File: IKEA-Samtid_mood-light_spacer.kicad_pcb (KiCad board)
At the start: 2 copper layers, 65 x 65 mm, 2 parts, among them P3.1 B-to-B-1A, P4.1 B-to-B-2A

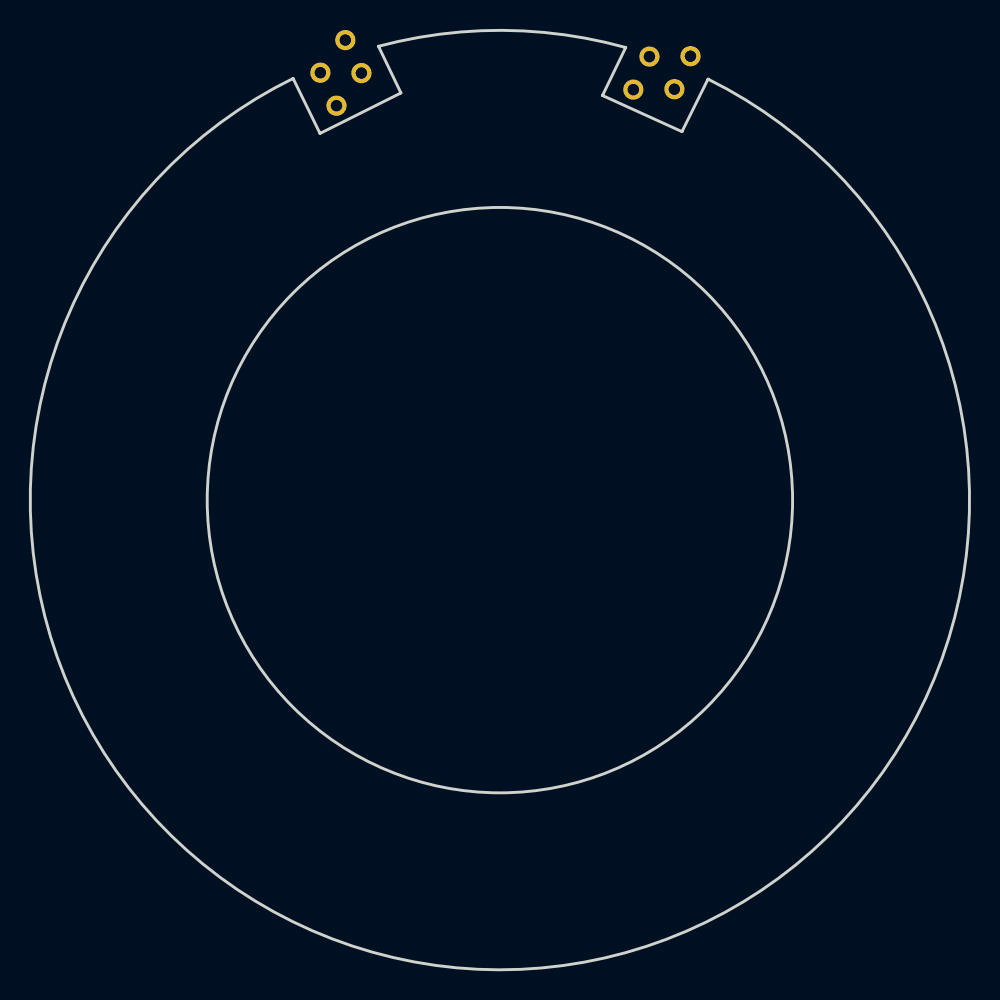
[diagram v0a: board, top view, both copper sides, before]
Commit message: Updated the spacer board outline.
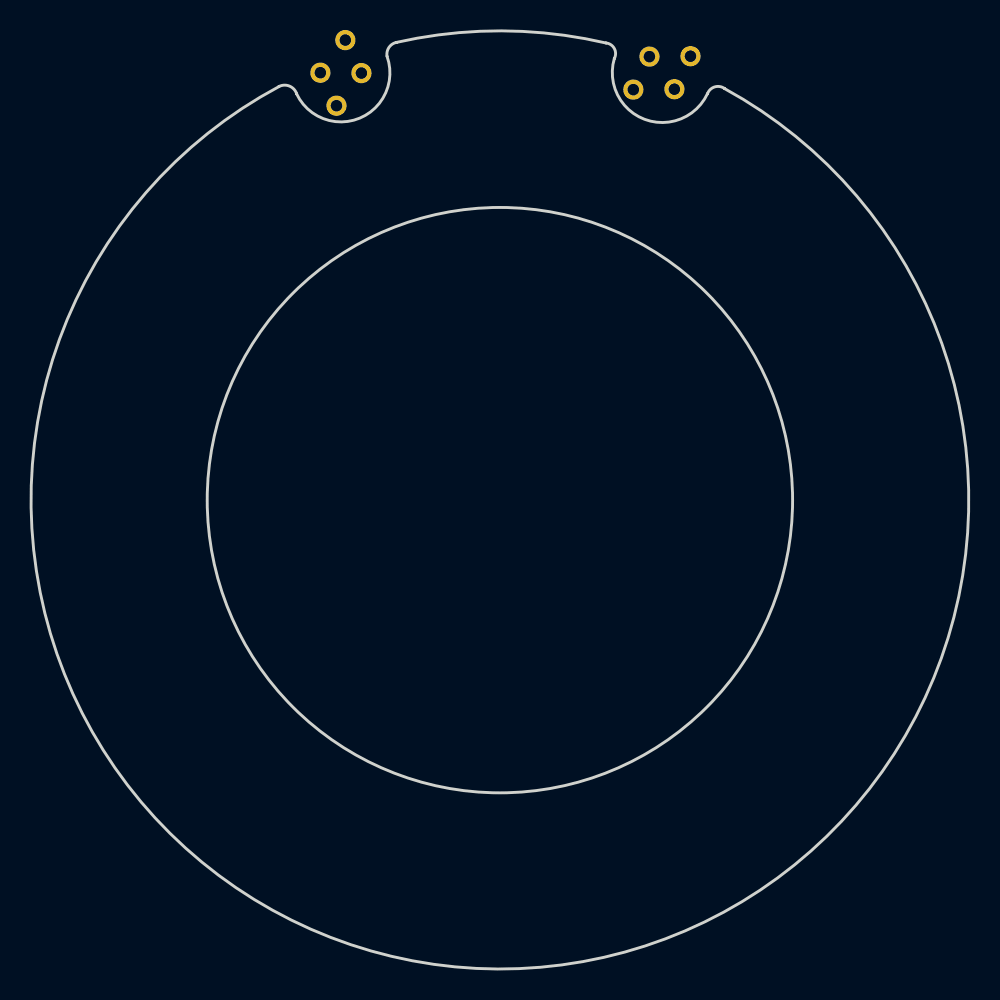
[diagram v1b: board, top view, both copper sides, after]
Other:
- board size 65 x 65 mm -> 64.9 x 64.9 mm
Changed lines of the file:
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@@
     (links 0)
     (no_connects 0)
-    (area 117.399999 60.875732 182.600001 127.600001)
+    (area 117.460156 62.430714 182.539844 127.539844)
     (thickness 1.6)
     (drawings 11)
@@
     (pad 4 thru_hole circle (at -1.905 -1.27 116) (size 1.4 1.4) (drill 0.8) (layers *.Cu *.Mask))
   )
-  (gr_arc (start 150 95) (end 141.6 63.6) (angle 30.51038738) (layer Edge.Cuts) (width 0.2))
-  (gr_line (start 143.153934 66.829267) (end 141.6 63.6) (layer Edge.Cuts) (width 0.2))
-  (gr_line (start 137.553745 69.627827) (end 143.153745 66.827827) (layer Edge.Cuts) (width 0.2))
-  (gr_line (start 157.098288 67.003506) (end 158.705371 63.682571) (layer Edge.Cuts) (width 0.2))
-  (gr_line (start 162.597965 69.50407) (end 157.097965 67.00407) (layer Edge.Cuts) (width 0.2))
-  (gr_line (start 162.597378 69.503251) (end 164.4 65.87) (layer Edge.Cuts) (width 0.2))
-  (gr_line (start 135.692554 65.824723) (end 137.553317 69.627554) (layer Edge.Cuts) (width 0.2))
-  (gr_arc (start 150 95) (end 164.4 65.87) (angle 307.5734628) (layer Edge.Cuts) (width 0.2))
+  (gr_arc (start 157.27 64.1) (end 157.34 63.37) (angle 113.4318231) (layer Edge.Cuts) (width 0.2))
+  (gr_arc (start 165.09 67.15) (end 164.36 66.89) (angle 106.7433869) (layer Edge.Cuts) (width 0.2))
+  (gr_arc (start 161.23 65.42) (end 164.36 66.88) (angle 171.4494212) (layer Edge.Cuts) (width 0.2))
+  (gr_arc (start 143.02 64.15) (end 142.19 64.28) (angle 87.05963669) (layer Edge.Cuts) (width 0.2))
+  (gr_arc (start 135.11 67.16) (end 134.7 66.39) (angle 100.818031) (layer Edge.Cuts) (width 0.2))
+  (gr_arc (start 139 65.44) (end 142.19 64.29) (angle 174.6054151) (layer Edge.Cuts) (width 0.2))
+  (gr_arc (start 150 95) (end 142.84 63.33) (angle 25.80990109) (layer Edge.Cuts) (width 0.2))
+  (gr_arc (start 150 95) (end 165.55 66.53) (angle 303.2441293) (layer Edge.Cuts) (width 0.2))
   (gr_circle (center 150 95) (end 150.5 95) (layer Eco1.User) (width 0.2))
   (gr_circle (center 150 95) (end 170.25 95) (layer Edge.Cuts) (width 0.2))

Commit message: Swapped male / female micro-MaTch connectors. Adjusted spacer board.
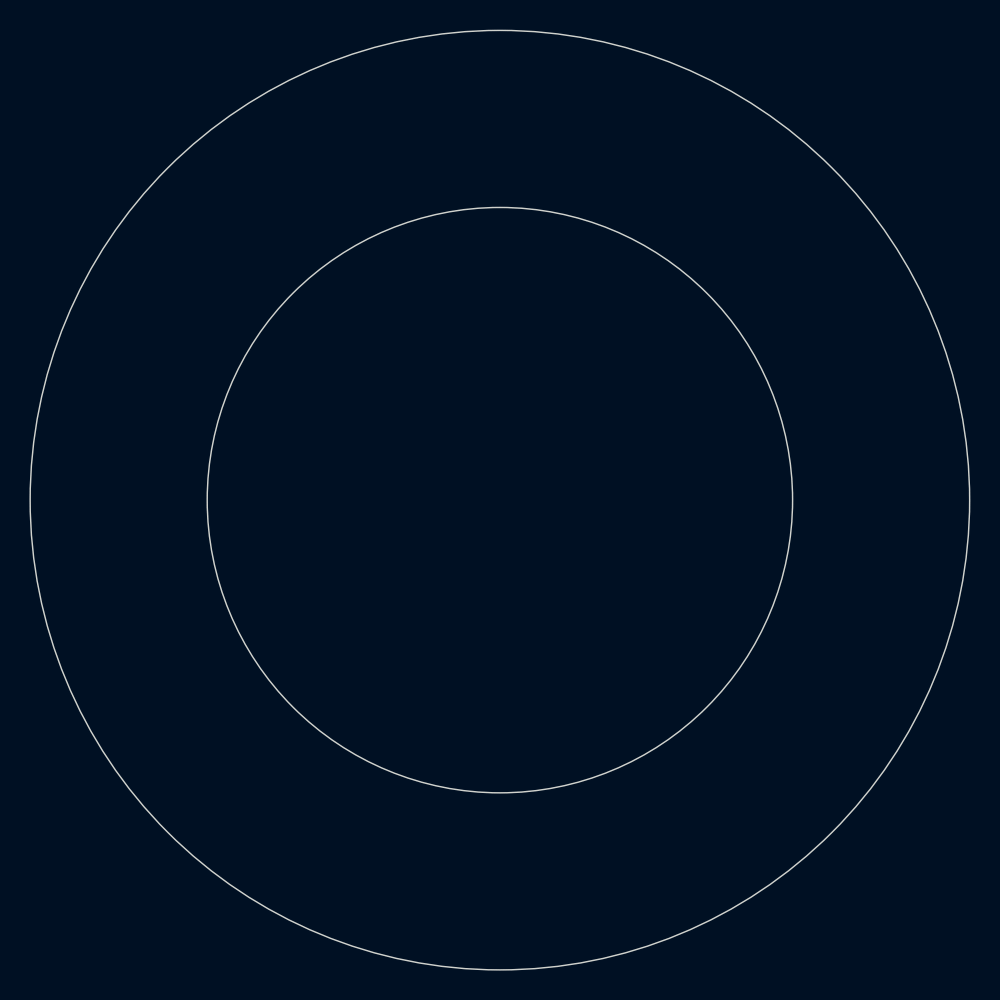
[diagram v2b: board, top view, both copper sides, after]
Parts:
- removed P3.1: B-to-B-1A, con-amp-micromatch-MICROMATCH-4
- removed P4.1: B-to-B-2A, con-amp-micromatch-MICROMATCH-4
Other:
- board size 64.9 x 64.9 mm -> 65 x 65 mm
